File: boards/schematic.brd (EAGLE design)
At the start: 83.5 x 86.3 mm, 106 parts, among them IC1 74LS165D, J1 AVR_SPI_PRG_6NS, Q1 MOSFET-NCHANNELBSS123LT1G, U1 SD_CARD_SOCKET, U2 SD_CARD_SOCKET, U3 LCD-16X2SILK, U4 MAX1555

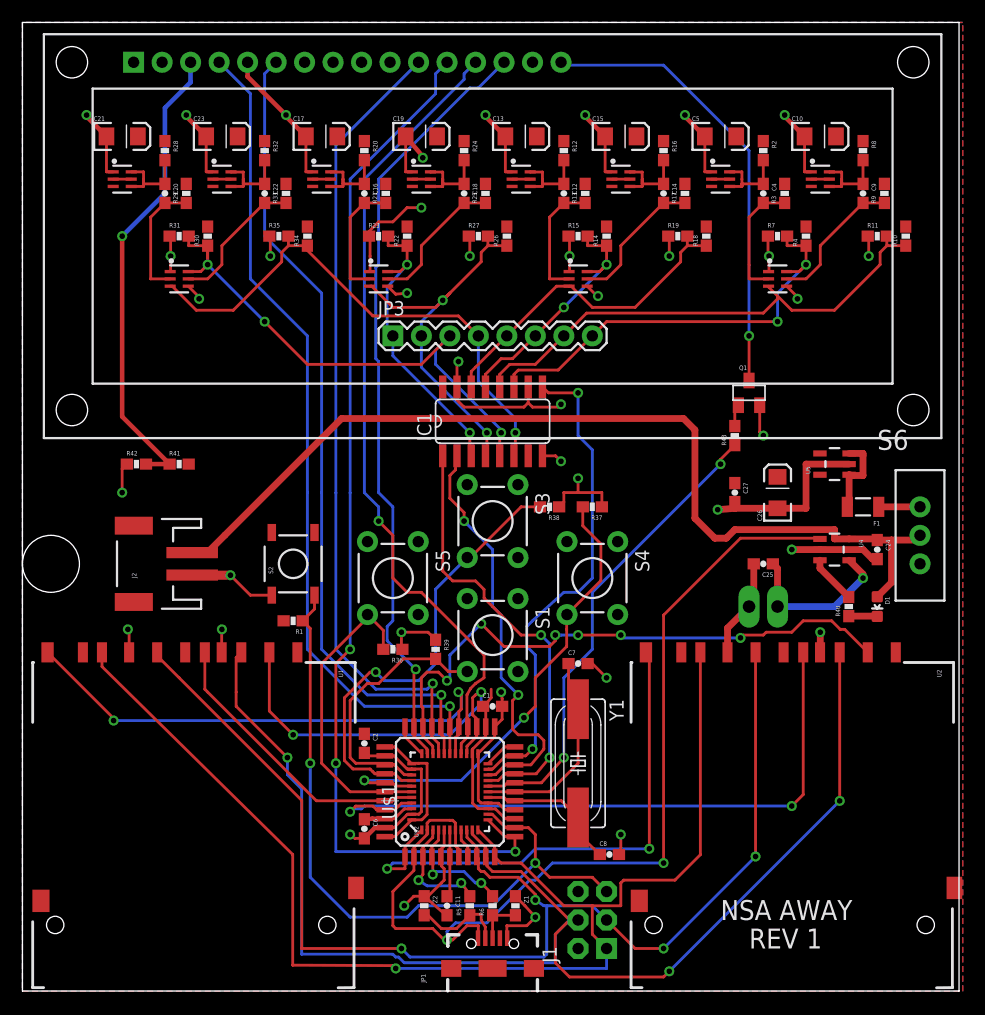
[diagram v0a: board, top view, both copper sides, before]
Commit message: Improvements to the enclosure, tweaking the PCB
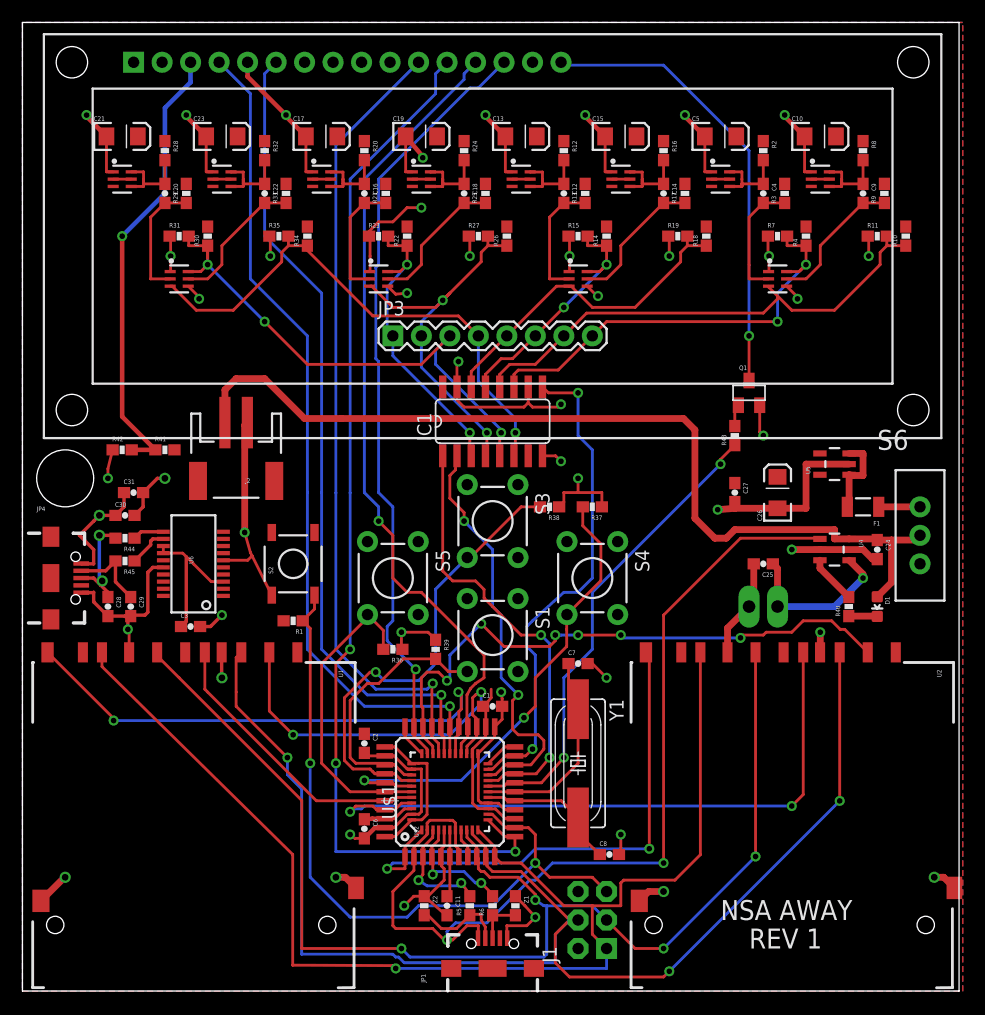
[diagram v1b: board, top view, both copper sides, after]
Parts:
- added C28, C29: 47pf, SparkFun-Passives:0603-CAP
- added C3, C30: .1uF, SparkFun-Passives:0603-CAP
- added C31: 4.7uF, SparkFun-Passives:0603-CAP
- added JP4: USB_MICROB_PLUGCONN-11752, SparkFun-Connectors:USB-B-MICRO-SMD_V03
- added R44, R45: 22, SparkFun-Passives:0603-RES
- added U6: FTS31XS-U, SparkFun-DigitalIC:SSOP20_L
- moved J2 11.7 mm to (19.1, 47.0), turned to 180 degrees
- moved R41 1.80 mm to (12.7, 48.3)
- moved R42 1.80 mm to (8.89, 48.3)
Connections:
- new net +5V: C30.1, C31.1, JP4.VBUS1, U6.15
- new net N$22: C28.1, JP4.D+1, R44.2
- new net N$23: C29.1, JP4.D-1, R45.2
- new net N$37: R44.1, U6.11
- new net N$38: R45.1, U6.12
- new net N$40: C3.1, U6.13, U6.14, U6.3
- new net POS_RX_LOGIC: U6.20
- new net POS_TX_LOGIC: U6.4
- net GND: now also C28.2, C29.2, C3.2, C30.2, C31.2, JP4.GND1, U1.SH@1, U1.SH@2, U2.SH@1, U2.SH@2, U6.16, U6.6
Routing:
- net GND: track 224.8 -> 266.6 mm, vias 39 -> 45
- net N$40: track 0.00 -> 13.5 mm
- net +5V: track 0.00 -> 10.7 mm, vias 0 -> 1
- net N$22: track 0.00 -> 9.47 mm, vias 0 -> 2
- net N$23: track 0.00 -> 7.19 mm
- net N$38: track 0.00 -> 3.58 mm
- net N$3: track 85.8 -> 82.7 mm
- net N$37: track 0.00 -> 2.80 mm
- net N$39: track 42.2 -> 40.4 mm
